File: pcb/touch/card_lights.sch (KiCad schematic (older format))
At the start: 6 parts, among them SW1 SW_Push

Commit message: create touch PCB
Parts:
- removed SW1: SW_Push, pl_Tactile_Switch_SMD:Bright_TSA123G60-250, symbol Switch:SW_Push
- removed TP1, TP2: TestPoint, TestPoint:TestPoint_Pad_4.0x4.0mm, symbol Connector:TestPoint
- added C1, C2: 100n, Capacitor_SMD:C_0603_1608Metric_Pad1.08x0.95mm_HandSolder, symbol Device:C
- added D1, D2, D3, D4, D5, D6: LED, symbol Device:LED
- added J1: TOUCH PAD, TestPoint:TestPoint_THTPad_D2.0mm_Drill1.0mm, symbol pl_tontek_touch_controller:touch_pad
- added J2, J3, J4: LED_PAD, TestPoint:TestPoint_Pad_4.0x4.0mm, symbol Connector:Conn_01x01_Male
- added J5, J6, J7: LED_WIRE, symbol Connector:Conn_01x01_Female
- added R3: 91, Resistor_SMD:R_0603_1608Metric_Pad0.98x0.95mm_HandSolder, symbol Device:R
- added U1: ATtiny10-TS, Package_TO_SOT_SMD:SOT-23-6_Handsoldering, symbol MCU_Microchip_ATtiny:ATtiny10-TS
- added U2: TTP223E-HA6, Package_TO_SOT_SMD:SOT-23-6_Handsoldering, symbol pl_tontek_touch_controller:TTP223E-HA6
- R1, R2: value 1k -> 91
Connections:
- net labels added: +3V0, PB0, PB1, PB2, PB3, TOUCH
- wire segments 16 -> 61
- no-connect marks 0 -> 1
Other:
- note added: "ERC Happy Area"
- note added: "Offboard Charlieplex LEDs Wired Using Pads"
- note added: "PULL TOG HIGH TO TOGGLE OUTPUT\nCURRENT DRAW SEEMS THE SAME FOR BOTH MODES\nEASIER IN CODE TO TOGGLE"
- note added: "THIS AREA FOR REFERENCE ONLY"
- note removed: "Solder String LED to TP"
- moved on the sheet: BT1, R1, R2

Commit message: add touch sensitivity adjustment capacitor
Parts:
- added C?: 10p, Capacitor_SMD:C_0603_1608Metric_Pad1.08x0.95mm_HandSolder, symbol Device:C
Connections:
- net GND: now also C?.2
- net TOUCH: now also C?.1
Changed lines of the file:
@@
 $EndComp
 Wire Wire Line
-	6700 2400 7700 2400
+	6700 2400 7500 2400
 Text Label 7000 2400 2    50   ~ 0
 TOUCH
@@
 Text Notes 9000 5700 2    50   ~ 0
 THIS AREA FOR REFERENCE ONLY
+$Comp
+L Device:C C?
+U 1 1 5FEE0F0C
+P 7500 2650
+F 0 "C?" H 7525 2750 50  0000 L CNN
+F 1 "10p" H 7525 2550 50  0000 L CNN
+F 2 "Capacitor_SMD:C_0603_1608Metric_Pad1.08x0.95mm_HandSolder" H 7538 2500 50  0001 C CNN
+F 3 "~" H 7500 2650 50  0001 C CNN
+	1    7500 2650
+	1    0    0    -1
+$EndComp
+Wire Wire Line
+	7500 2500 7500 2400
+Connection ~ 7500 2400
+Wire Wire Line
+	7500 2400 7700 2400
+$Comp
+L power:GND #PWR?
+U 1 1 5FEE26DA
+P 7500 2850
+F 0 "#PWR?" H 7500 2600 50  0001 C CNN
+F 1 "GND" H 7500 2700 50  0000 C CNN
+F 2 "" H 7500 2850 50  0001 C CNN
+F 3 "" H 7500 2850 50  0001 C CNN
+	1    7500 2850
+	1    0    0    -1
+$EndComp
+Wire Wire Line
+	7500 2850 7500 2800
 $EndSCHEMATC

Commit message: annotations
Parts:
- gave numbers to parts that had none: 1
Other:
- note added: "For touch pad use flood fill on PCB back"
- note added: "Use C3 to adjust touch sensitivity\n1pF to 50pF suggested in datasheet\n10pF seems to be about right in prototype testing"
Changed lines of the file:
@@
 THIS AREA FOR REFERENCE ONLY
 $Comp
-L Device:C C?
+L Device:C C3
 U 1 1 5FEE0F0C
 P 7500 2650
-F 0 "C?" H 7525 2750 50  0000 L CNN
+F 0 "C3" H 7525 2750 50  0000 L CNN
 F 1 "10p" H 7525 2550 50  0000 L CNN
 F 2 "Capacitor_SMD:C_0603_1608Metric_Pad1.08x0.95mm_HandSolder" H 7538 2500 50  0001 C CNN
@@
 	7500 2400 7700 2400
 $Comp
-L power:GND #PWR?
+L power:GND #PWR06
 U 1 1 5FEE26DA
 P 7500 2850
-F 0 "#PWR?" H 7500 2600 50  0001 C CNN
+F 0 "#PWR06" H 7500 2600 50  0001 C CNN
 F 1 "GND" H 7500 2700 50  0000 C CNN
 F 2 "" H 7500 2850 50  0001 C CNN
@@
 Wire Wire Line
 	7500 2850 7500 2800
+Wire Notes Line style solid
+	7000 3500 9000 3500
+Wire Notes Line style solid
+	9000 3500 9000 3250
+Wire Notes Line style solid
+	9000 3250 7000 3250
+Text Notes 7500 1850 0    50   ~ 0
+Use C3 to adjust touch sensitivity\n1pF to 50pF suggested in datasheet\n10pF seems to be about right in prototype testing
+Wire Notes Line style solid
+	7500 2350 7500 1600
+Wire Notes Line style solid
+	7500 1600 9450 1600
+Wire Notes Line style solid
+	9450 1600 9450 1850
+Wire Notes Line style solid
+	9450 1850 7500 1850
+Wire Notes Line style solid
+	7000 3050 7000 3500
+Text Notes 8850 2450 0    50   ~ 0
+For touch pad use flood fill on PCB back
 $EndSCHEMATC

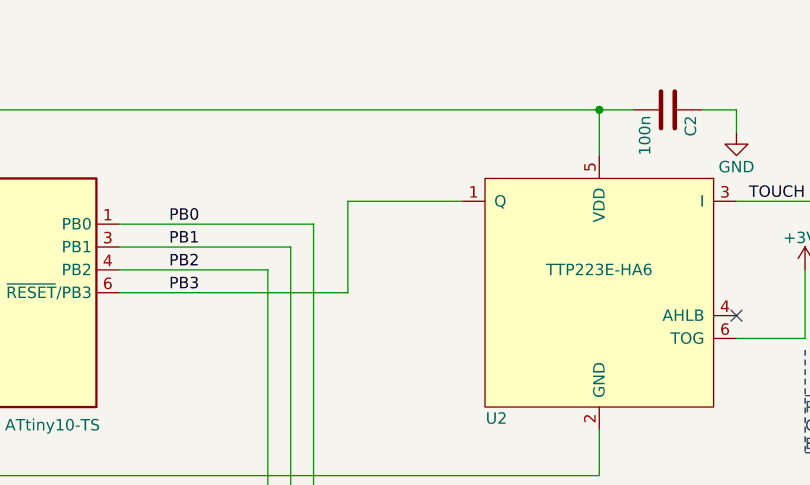
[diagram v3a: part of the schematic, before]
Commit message: add diode to RESET for insystem HV programming that does not damage TTP223E
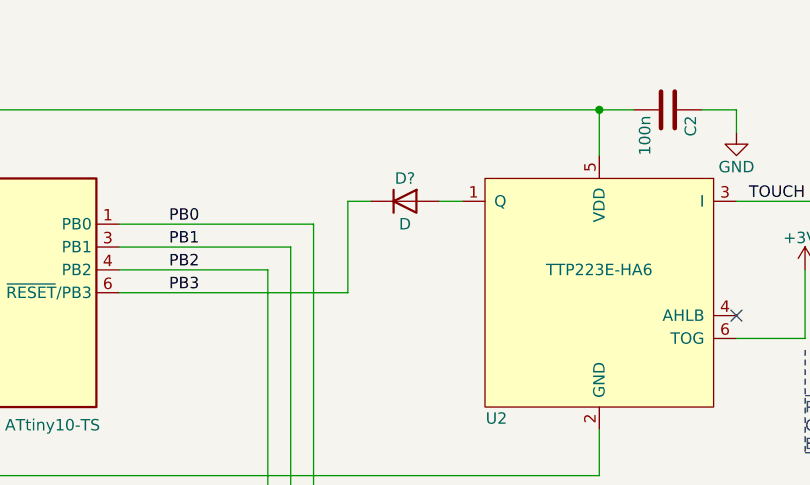
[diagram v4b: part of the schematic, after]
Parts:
- added D?: D, symbol Device:D
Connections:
- net PB3: now also D?.1 (K); no longer U2.1 (Q)
- new net: D?.2 (A), U2.1 (Q)
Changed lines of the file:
@@
 Wire Wire Line
 	5000 2800 5000 2400
-Wire Wire Line
-	5000 2400 5500 2400
 Text Label 4350 2800 2    50   ~ 0
 PB3
@@
 Text Notes 8850 2450 0    50   ~ 0
 For touch pad use flood fill on PCB back
+$Comp
+L Device:D D?
+U 1 1 5FF0713E
+P 5250 2400
+F 0 "D?" H 5250 2500 50  0000 C CNN
+F 1 "D" H 5250 2300 50  0000 C CNN
+F 2 "" H 5250 2400 50  0001 C CNN
+F 3 "~" H 5250 2400 50  0001 C CNN
+	1    5250 2400
+	1    0    0    -1
+$EndComp
+Wire Wire Line
+	5000 2400 5100 2400
+Wire Wire Line
+	5400 2400 5500 2400
 $EndSCHEMATC

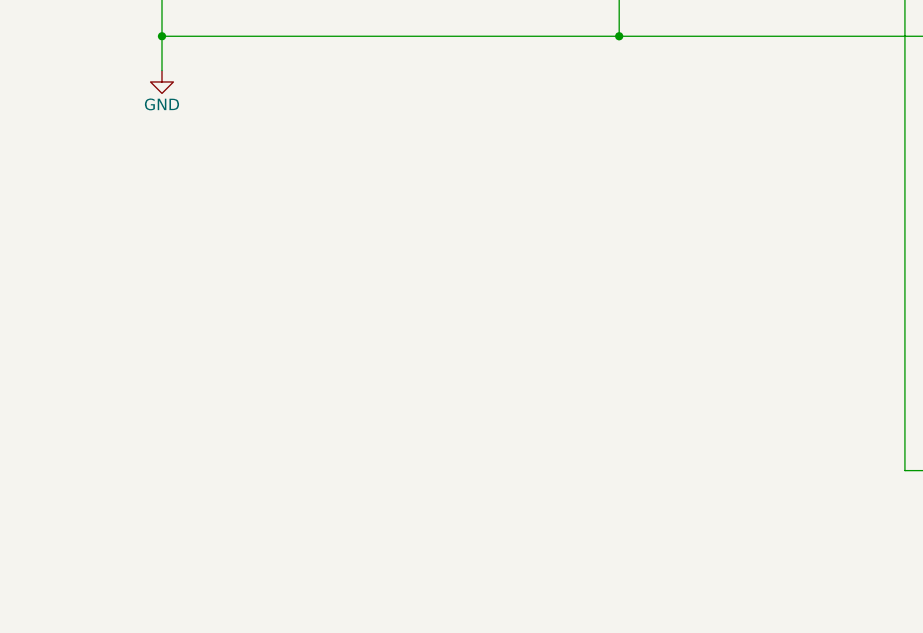
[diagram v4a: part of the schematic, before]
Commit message: add test points for in system programming
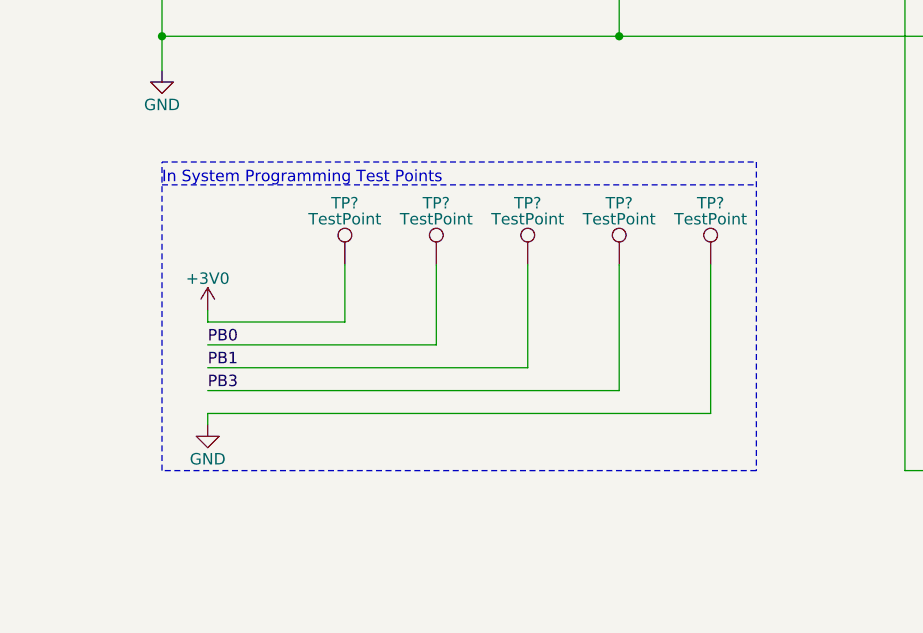
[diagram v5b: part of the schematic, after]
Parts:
- added TP? (x5): TestPoint, symbol Connector:TestPoint
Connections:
- net +3V0: now also TP?.1
- net GND: now also TP?.1
- net PB0: now also TP?.1
- net PB1: now also TP?.1
- net PB3: now also TP?.1
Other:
- note added: "In System Programming Test Points"
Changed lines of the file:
@@
 Sheet 1 1
 Title "Touch Card Lights"
-Date "2020-12-19"
-Rev ""
+Date "2020-12-31"
+Rev "A"
 Comp "Perry Leumas"
 Comment1 ""
@@
 Wire Wire Line
 	5400 2400 5500 2400
+$Comp
+L Connector:TestPoint TP?
+U 1 1 5FF0CDEF
+P 3400 4600
+F 0 "TP?" H 3400 4870 50  0000 C CNN
+F 1 "TestPoint" H 3400 4800 50  0000 C CNN
+F 2 "" H 3600 4600 50  0001 C CNN
+F 3 "~" H 3600 4600 50  0001 C CNN
+	1    3400 4600
+	1    0    0    -1
+$EndComp
+$Comp
+L Connector:TestPoint TP?
+U 1 1 5FF0DBF1
+P 3800 4600
+F 0 "TP?" H 3800 4870 50  0000 C CNN
+F 1 "TestPoint" H 3800 4800 50  0000 C CNN
+F 2 "" H 4000 4600 50  0001 C CNN
+F 3 "~" H 4000 4600 50  0001 C CNN
+	1    3800 4600
+	1    0    0    -1
+$EndComp
+$Comp
+L Connector:TestPoint TP?
+U 1 1 5FF0DEB0
+P 3000 4600
+F 0 "TP?" H 3000 4870 50  0000 C CNN
+F 1 "TestPoint" H 3000 4800 50  0000 C CNN
+F 2 "" H 3200 4600 50  0001 C CNN
+F 3 "~" H 3200 4600 50  0001 C CNN
+	1    3000 4600
+	1    0    0    -1
+$EndComp
+$Comp
+L Connector:TestPoint TP?
+U 1 1 5FF0E406
+P 2200 4600
+F 0 "TP?" H 2200 4870 50  0000 C CNN
+F 1 "TestPoint" H 2200 4800 50  0000 C CNN
+F 2 "" H 2400 4600 50  0001 C CNN
+F 3 "~" H 2400 4600 50  0001 C CNN
+	1    2200 4600
+	1    0    0    -1
+$EndComp
+Text Label 1600 4950 0    50   ~ 0
+PB0
+Text Label 1600 5050 0    50   ~ 0
+PB1
+Text Label 1600 5150 0    50   ~ 0
+PB3
+$Comp
+L power:+3V0 #PWR?
+U 1 1 5FF139D5
+P 1600 4800
+F 0 "#PWR?" H 1600 4650 50  0001 C CNN
+F 1 "+3V0" H 1600 4940 50  0000 C CNN
+F 2 "" H 1600 4800 50  0001 C CNN
+F 3 "" H 1600 4800 50  0001 C CNN
+	1    1600 4800
+	1    0    0    -1
+$EndComp
+$Comp
+L power:GND #PWR?
+U 1 1 5FF13F03
+P 1600 5300
+F 0 "#PWR?" H 1600 5050 50  0001 C CNN
+F 1 "GND" H 1600 5150 50  0000 C CNN
+F 2 "" H 1600 5300 50  0001 C CNN
+F 3 "" H 1600 5300 50  0001 C CNN
+	1    1600 5300
+	1    0    0    -1
+$EndComp
+$Comp
+L Connector:TestPoint TP?
+U 1 1 5FF35544
+P 2600 4600
+F 0 "TP?" H 2600 4870 50  0000 C CNN
+F 1 "TestPoint" H 2600 4800 50  0000 C CNN
+F 2 "" H 2800 4600 50  0001 C CNN
+F 3 "~" H 2800 4600 50  0001 C CNN
+	1    2600 4600
+	1    0    0    -1
+$EndComp
+Wire Wire Line
+	1600 4950 2600 4950
+Wire Wire Line
+	2600 4950 2600 4600
+Wire Wire Line
+	1600 5050 3000 5050
+Wire Wire Line
+	3000 5050 3000 4600
+Wire Wire Line
+	1600 5150 3400 5150
+Wire Wire Line
+	3400 5150 3400 4600
+Wire Wire Line
+	1600 4800 1600 4850
+Wire Wire Line
+	1600 4850 2200 4850
+Wire Wire Line
+	2200 4850 2200 4600
+Wire Wire Line
+	1600 5300 1600 5250
+Wire Wire Line
+	1600 5250 3800 5250
+Wire Wire Line
+	3800 5250 3800 4600
+Text Notes 1400 4250 0    50   ~ 0
+In System Programming Test Points
+Wire Notes Line
+	1400 4250 4000 4250
+Wire Notes Line
+	4000 5500 1400 5500
+Wire Notes Line
+	1400 5500 1400 4150
+Wire Notes Line
+	1400 4150 4000 4150
+Wire Notes Line
+	4000 4150 4000 5500
 $EndSCHEMATC
